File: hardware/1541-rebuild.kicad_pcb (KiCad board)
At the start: 2 copper layers, 76.2 x 97.8 mm, 30 parts, among them IC1 ATMEGA1284P-P, IC2 VIA6522, J1 ISP, J2 KEYS, J3 EXT_5V, J4 RESET CONN, J5 PC7, J6 LCD Display, P1 VIA_PIN_1-20, P2 VIA_PIN_21-40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

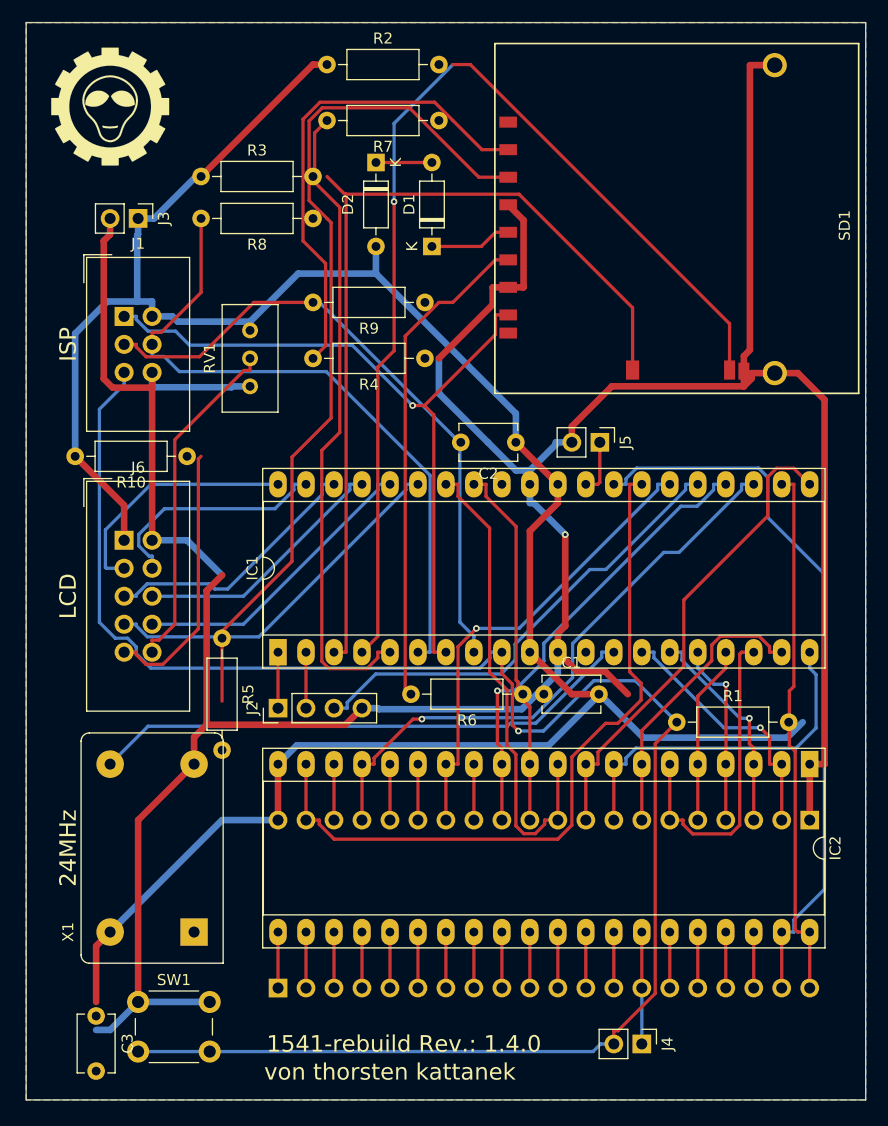
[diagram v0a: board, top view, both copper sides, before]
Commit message: Schaltplan angepasst: - SD Card Slot entfernt - SD Card Modul Connector hinzugefügt - im PCB alle Leiterbahne entfernt
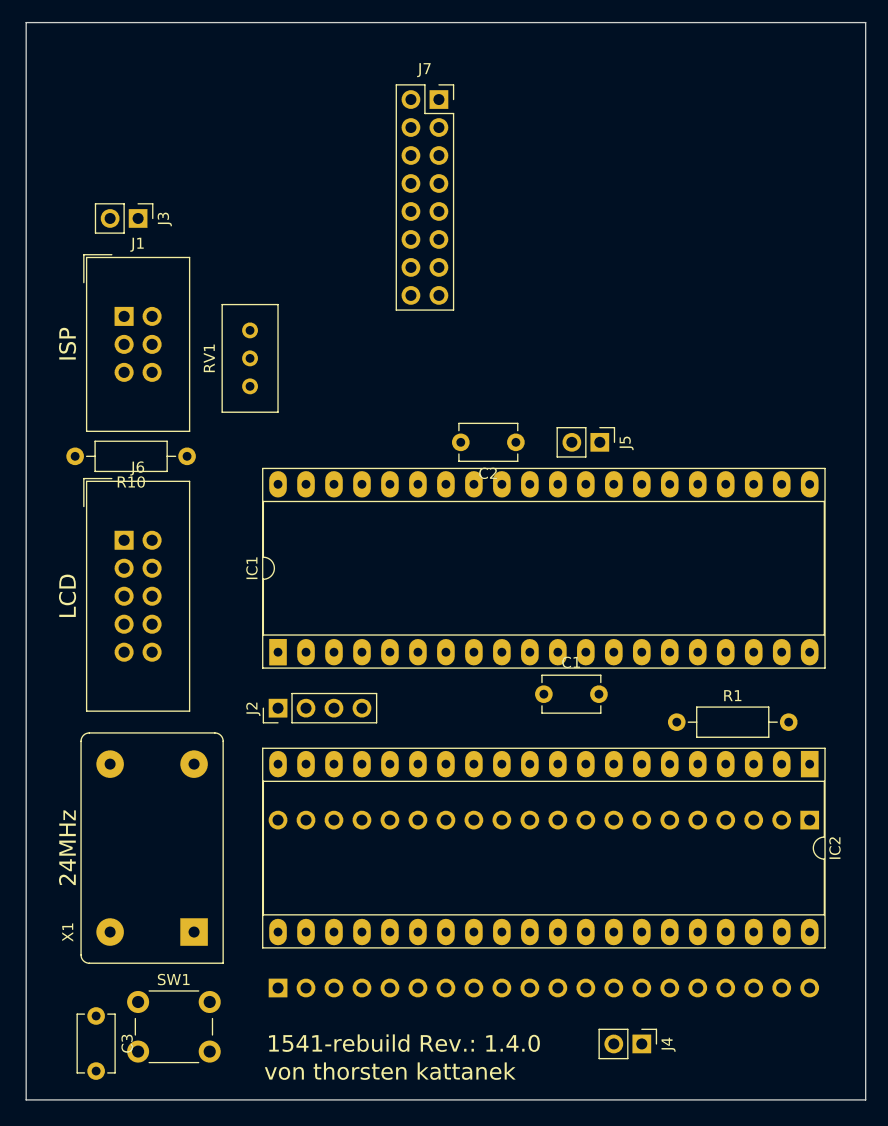
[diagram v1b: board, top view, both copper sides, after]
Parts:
- removed D1, D2: 1N4148, Diode_THT:D_DO-35_SOD27_P7.62mm_Horizontal
- removed G***: LOGO, logos_tk:logo_01_10_7mm_fsilk
- removed R2, R3: 47k, Resistor_THT:R_Axial_DIN0207_L6.3mm_D2.5mm_P10.16mm_Horizontal
- removed R4, R5, R6: 3,3k, Resistor_THT:R_Axial_DIN0207_L6.3mm_D2.5mm_P10.16mm_Horizontal
- removed R7, R8, R9: 1,8k, Resistor_THT:R_Axial_DIN0207_L6.3mm_D2.5mm_P10.16mm_Horizontal
- removed SD1: ATTEND_104H-TDA0-R01, sd_sockets_tk:ATTEND_104H-TDA0-R01
- added J7: SD Card Modul Connector, Connector_PinSocket_2.54mm:PinSocket_2x08_P2.54mm_Vertical, F.Cu at (145.4, 48.9)
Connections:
- net /SD Karte/MISO renamed MISO
- net /SD Karte/MOSI renamed MOSI
- net /SD Karte/SCK renamed SCK
- IC1 pad 3: /SD Karte/SD_DETECT -> /SD_DETECT
- IC1 pad 4: /SD Karte/SD_WP -> /SD_WP
- IC1 pad 5: /SD Karte/SS -> CS
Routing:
- net GND: track 417.5 -> 0.00 mm, vias 1 -> 0
- net +5V: track 220.3 -> 0.00 mm
- net Net-(IC1-Pad9): track 164.0 -> 0.00 mm, vias 1 -> 0
- net /SD Karte/SD_WP: track 95.8 -> 0.00 mm, vias 1 -> 0
- net /SD Karte/SD_DETECT: track 81.0 -> 0.00 mm
- net MISO: track 66.7 -> 0.00 mm, vias 1 -> 0
- net /VIA 6522 Sockel/OE: track 66.4 -> 0.00 mm
- net /VIA 6522 Sockel/SOE: track 66.0 -> 0.00 mm
- net MOSI: track 61.7 -> 0.00 mm
- net /SD Karte/SS: track 58.5 -> 0.00 mm
- net SCK: track 57.9 -> 0.00 mm
- net /VIA 6522 Sockel/SYNC: track 53.6 -> 0.00 mm, vias 1 -> 0
- net Net-(IC1-Pad13): track 50.2 -> 0.00 mm
- net /VIA 6522 Sockel/BRDY: track 48.4 -> 0.00 mm
- net Net-(R6-Pad2): track 44.9 -> 0.00 mm
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- removed copper zone on B.Cu, net GND
- removed copper zone on F.Cu, net GND

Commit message: Platine geändert - größe angepasst für 1541 I + II - Bauteile neu angeordnet - Beschriftungen hinzugefügt
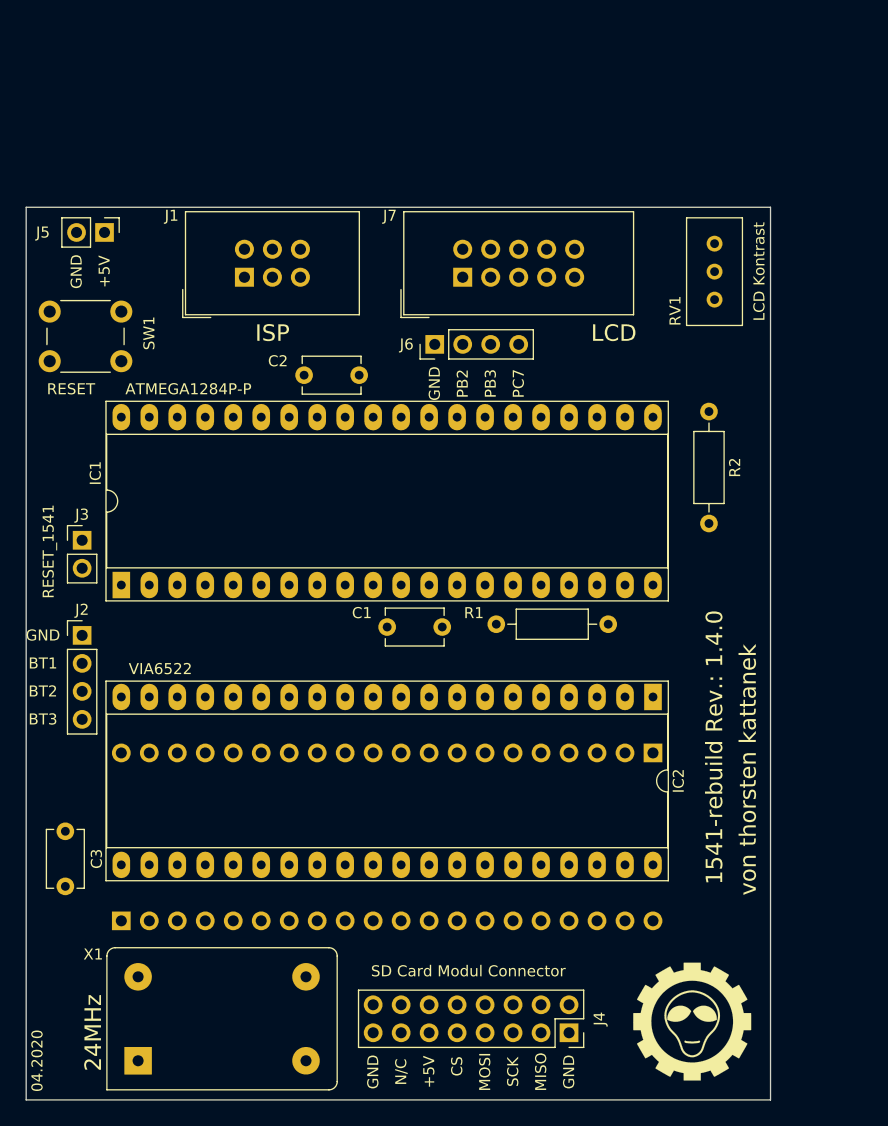
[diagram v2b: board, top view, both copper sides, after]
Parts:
- removed the J3 at (118.1, 59.7)
- removed the J7 at (145.4, 48.9)
- added G***: LOGO, logos_tk:logo_01_10_7mm_fsilk, F.Cu at (168.4, 132.6)
- added J4: SD Card Modul Connector, Connector_PinSocket_2.54mm:PinSocket_2x08_P2.54mm_Vertical, F.Cu at (157.2, 133.6)
- added J6: IO, Connector_PinHeader_2.54mm:PinHeader_1x04_P2.54mm_Vertical, F.Cu at (145.0, 71.1)
- J3: renamed from J4; value RESET CONN -> RESET_1541
- J5: value PC7 -> EXT_5V
- moved J3 68.3 mm to (113.0, 88.9), turned to 0 degrees
- moved SW1 58.2 mm to (116.6, 72.6), turned to 180 degrees
- moved J5 48.8 mm to (115.1, 61.0)
- moved R2 47.5 mm to (169.9, 77.2), turned to 270 degrees
- moved RV1 42.3 mm to (170.4, 67.1), turned to 270 degrees
- moved J7 38.9 mm to (147.6, 65.0), turned to 90 degrees
- moved J2 19.0 mm to (113.0, 97.5), turned to 0 degrees
- moved R1 18.6 mm to (150.6, 96.5)
- moved C3 17.0 mm to (111.5, 115.3)
- moved C2 15.5 mm to (138.2, 73.9)
- moved IC1 15.5 mm to (116.6, 93.0)
- moved P2 15.5 mm to (116.6, 123.4)
- moved C1 15.5 mm to (140.7, 96.8)
- moved IC2 15.5 mm to (164.8, 103.1)
- moved P1 15.5 mm to (164.8, 108.2)
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- renumbered J6 to J7, R10 to R2
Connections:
- IC1 pad 1: Net-(IC1-Pad1) -> /BT1
- IC1 pad 2: Net-(IC1-Pad2) -> /BT2
- IC1 pad 25: Net-(IC1-Pad25) -> /BT3
- IC1 pad 29: Net-(IC1-Pad29) -> PC7
- IC1 pad 3: /SD_DETECT -> PB2
- IC1 pad 4: /SD_WP -> PB3
- J2 pad 1: Net-(IC1-Pad1) -> GND
- J2 pad 2: Net-(IC1-Pad2) -> /BT1
- J2 pad 3: Net-(IC1-Pad25) -> /BT2
- J2 pad 4: GND -> /BT3
- J5 pad 1: Net-(IC1-Pad29) -> +5V
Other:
- board size 76.2 x 97.8 mm -> 67.6 x 81 mm
- board text added: "+5V"
- board text added: "04.2020"
- board text added: "BT1"
- board text added: "BT2"
- board text added: "BT3"
- board text added: "CS"
- board text added: "GND"
- board text added: "LCD Kontrast"
- board text added: "MISO"
- board text added: "MOSI"
- board text added: "N/C"
- board text added: "PB2"
- board text added: "PB3"
- board text added: "PC7"
- board text added: "SCK"

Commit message: Platine geändert - größe nochmals angepasst an 1541 II, 1541 kurz, 5141 mittel - Bauteile neu angeordnet
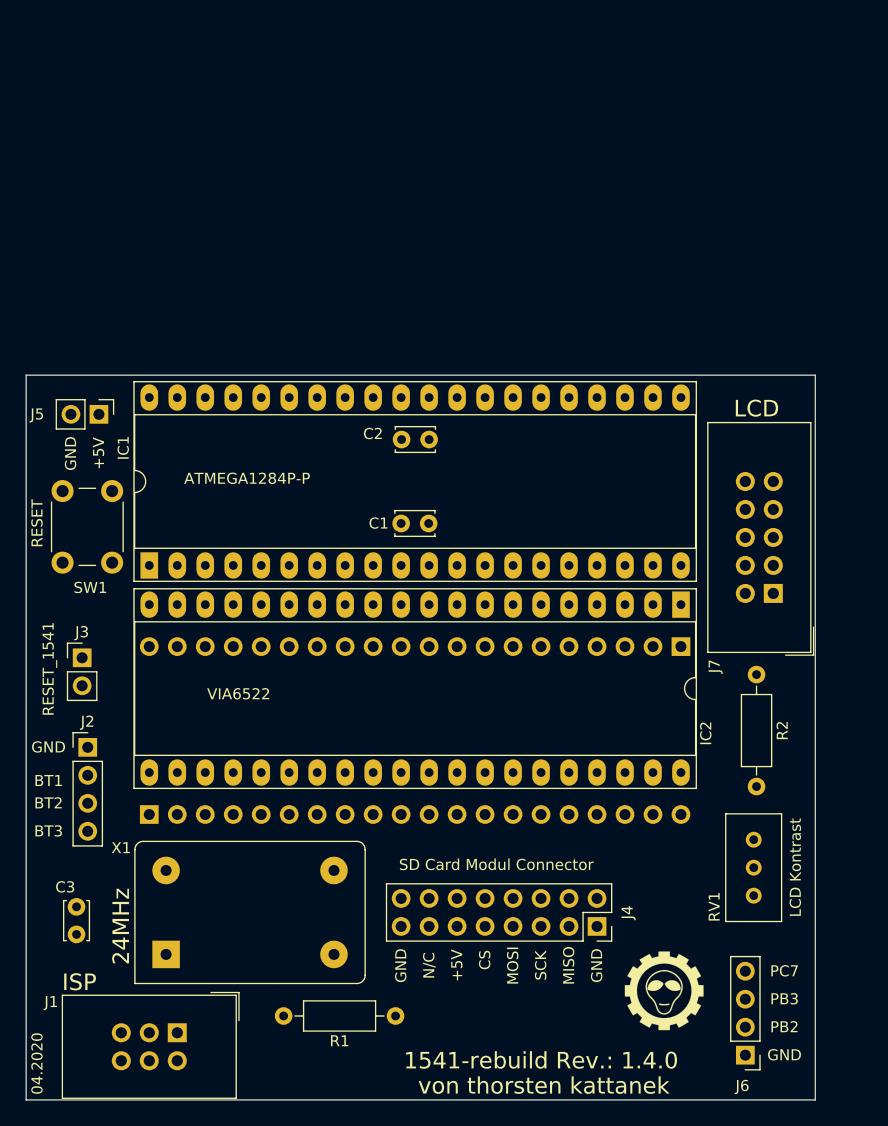
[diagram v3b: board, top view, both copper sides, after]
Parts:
- removed the G*** at (168.4, 132.6)
- added G***: LOGO, logos_tk:logo_01_7_1mm_fsilk, F.Cu at (165.9, 129.8)
- C1, C2, C3: footprint Capacitor_THT:C_Disc_D5.1mm_W3.2mm_P5.00mm -> Capacitor_THT:C_Disc_D3.4mm_W2.1mm_P2.50mm
- moved J6 70.4 mm to (173.2, 135.6), turned to 180 degrees
- moved J1 68.9 mm to (121.7, 133.6), turned to 270 degrees
- moved RV1 54.2 mm to (174.0, 121.2)
- moved R1 40.5 mm to (131.3, 132.1)
- moved J7 40.2 mm to (175.8, 93.7), turned to 180 degrees
- moved R2 24.3 mm to (174.2, 101.1)
- moved SW1 19.0 mm to (111.3, 90.9), turned to 90 degrees
- moved J5 16.5 mm to (114.6, 77.5)
- moved J3 10.7 mm to (113.0, 99.6)
- moved J2 10.2 mm to (113.5, 107.7)
- moved J4 9.98 mm to (159.8, 124.0)
- moved P2 9.98 mm to (119.1, 113.8)
- moved X1 9.98 mm to (120.7, 126.5)
- moved P1 9.98 mm to (167.4, 98.6)
- moved C1 9.48 mm to (142.0, 87.4)
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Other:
- board size 67.6 x 81 mm -> 71.6 x 65.8 mm

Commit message: DRC OK!
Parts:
- moved IC1 50.6 mm to (167.4, 75.9), turned to 270 degrees
- moved C2 0.25 mm to (144.5, 80.0)
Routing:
- net +5V: track 0.00 -> 213.9 mm, vias 0 -> 3
- net Net-(IC1-Pad9): track 0.00 -> 111.0 mm, vias 0 -> 5
- net MOSI: track 0.00 -> 97.9 mm
- net /BT1: track 0.00 -> 96.2 mm, vias 0 -> 1
- net /BT2: track 0.00 -> 95.4 mm, vias 0 -> 1
- net MISO: track 0.00 -> 91.0 mm
- net SCK: track 0.00 -> 90.7 mm
- net PB3: track 0.00 -> 74.7 mm, vias 0 -> 1
- net PC7: track 0.00 -> 72.9 mm, vias 0 -> 2
- net PB2: track 0.00 -> 70.9 mm
- net /VIA 6522 Sockel/BRDY: track 0.00 -> 62.0 mm
- net CS: track 0.00 -> 59.6 mm, vias 0 -> 1
- net /VIA 6522 Sockel/PA6: track 0.00 -> 54.8 mm
- net /VIA 6522 Sockel/PA5: track 0.00 -> 52.3 mm
- net /VIA 6522 Sockel/PA0: track 0.00 -> 52.2 mm
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- added copper zone on B.Cu, net GND
- added copper zone on F.Cu, net GND

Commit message: readme.md geändert - Text überarbeitet - neues Bild eingefügt
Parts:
- moved J1 0.25 mm to (121.7, 133.3)
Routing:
- net /BT2: track 95.4 -> 95.9 mm

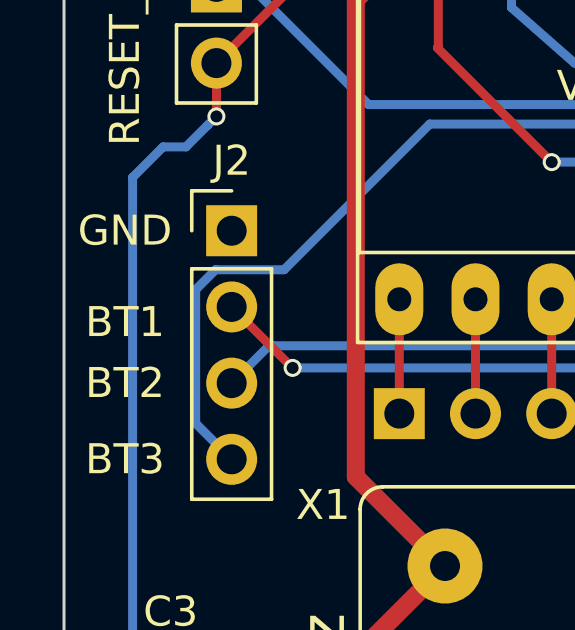
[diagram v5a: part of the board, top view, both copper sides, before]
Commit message: Platine geändert - link zum GitHub Repository als Beschriftung hinzugefügt
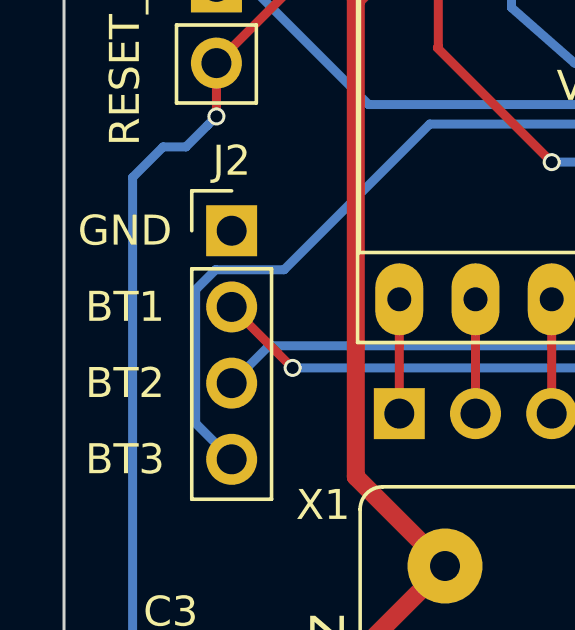
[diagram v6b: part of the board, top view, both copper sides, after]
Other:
- board text added: "https://github.com/ThKattanek/1541-rebuild"
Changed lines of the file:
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@@
   (general
     (thickness 1.6)
-    (drawings 29)
+    (drawings 30)
     (tracks 432)
     (zones 0)
@@
     )
   )
+  (gr_text https://github.com/ThKattanek/1541-rebuild (at 145.796 137.922) (layer B.SilkS)
+    (effects (font (size 1.5 1.5) (thickness 0.15)) (justify mirror))
+  )
   (gr_text 04.2020 (at 109.22 136.144 90) (layer F.SilkS)
     (effects (font (size 1 1) (thickness 0.15)))
@@
     (effects (font (size 1 1) (thickness 0.15)))
   )
-  (gr_text BT1 (at 109.982 110.744) (layer F.SilkS)
+  (gr_text BT1 (at 109.982 110.236) (layer F.SilkS)
     (effects (font (size 1 1) (thickness 0.15)))
   )
@@
     (connect_pads (clearance 0.508))
     (min_thickness 0.254)
-    (fill (arc_segments 32) (thermal_gap 0.508) (thermal_bridge_width 0.508))
+    (fill yes (arc_segments 32) (thermal_gap 0.508) (thermal_bridge_width 0.508))
     (polygon
       (pts
@@
     (connect_pads (clearance 0.508))
     (min_thickness 0.254)
-    (fill (arc_segments 32) (thermal_gap 0.508) (thermal_bridge_width 0.508))
+    (fill yes (arc_segments 32) (thermal_gap 0.508) (thermal_bridge_width 0.508))
     (polygon
       (pts

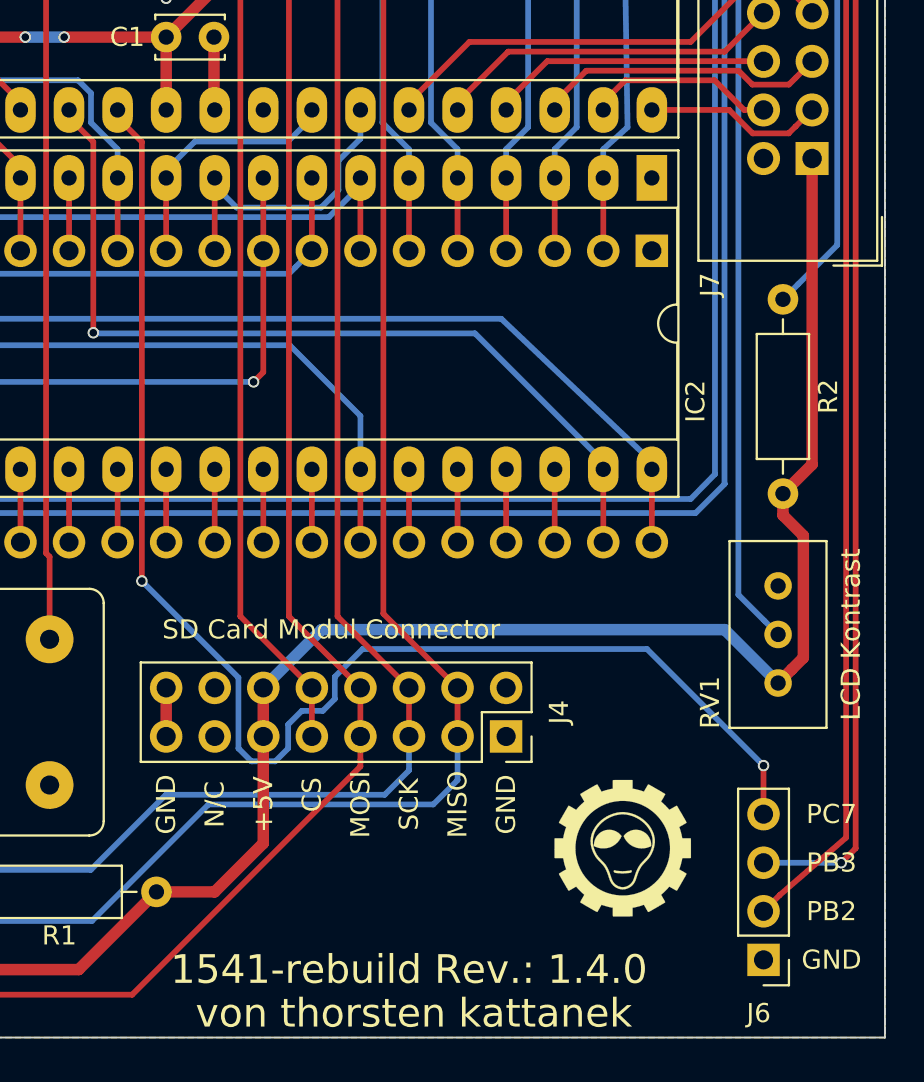
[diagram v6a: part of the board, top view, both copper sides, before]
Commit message: Platine geändert - Byte Ready Signal muss nicht mehr am GateArray durchtrennt werden - SOE zwischen VIA und VIA Pinheader getrennt - SOE des Pinheader geht zum PIN PC7 des Atmega
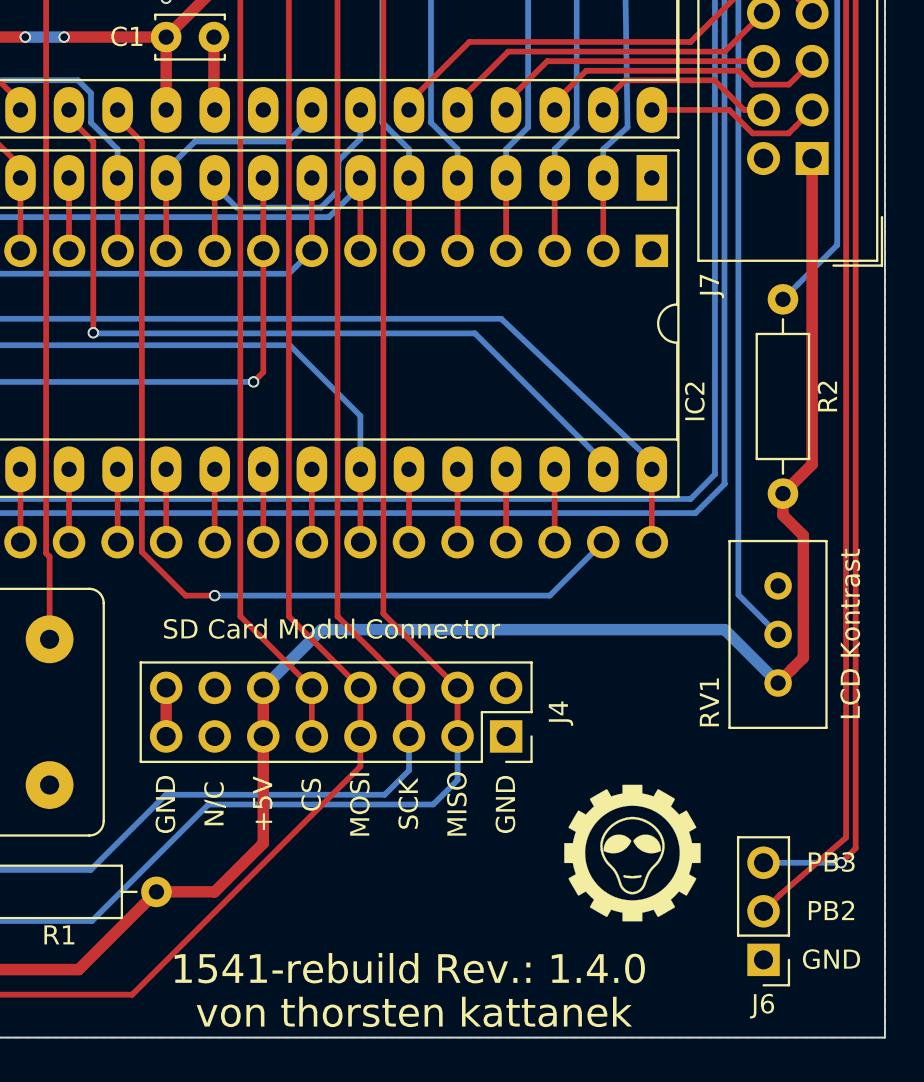
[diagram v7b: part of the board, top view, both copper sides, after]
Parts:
- J6: footprint Connector_PinHeader_2.54mm:PinHeader_1x04_P2.54mm_Vertical -> Connector_PinHeader_2.54mm:PinHeader_1x03_P2.54mm_Vertical
- moved G*** 0.57 mm to (166.4, 130.0)
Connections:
- IC1 pad 29: PC7 -> /VIA 6522 Sockel/SOE_GA
- P2 pad 19: /VIA 6522 Sockel/SOE -> /VIA 6522 Sockel/SOE_GA
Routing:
- net PC7: track 72.9 -> 0.00 mm, vias 2 -> 0
- net /VIA 6522 Sockel/SOE_GA: track 0.00 -> 49.9 mm, vias 0 -> 1
- net /VIA 6522 Sockel/SOE: track 45.8 -> 42.0 mm
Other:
- board text removed: "PC7"
